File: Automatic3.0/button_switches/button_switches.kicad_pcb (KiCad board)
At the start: 2 copper layers, 37 parts, among them J1 DB9_Female_MountingHoles, J2 Conn_01x01, J3 Conn_01x01, J4 Conn_01x01, J5 Conn_01x01, SW1 SW_DPST, SW2 SW_DPST, SW3 SW_DPST, SW4 SW_DPST, SW5 SW_DPST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

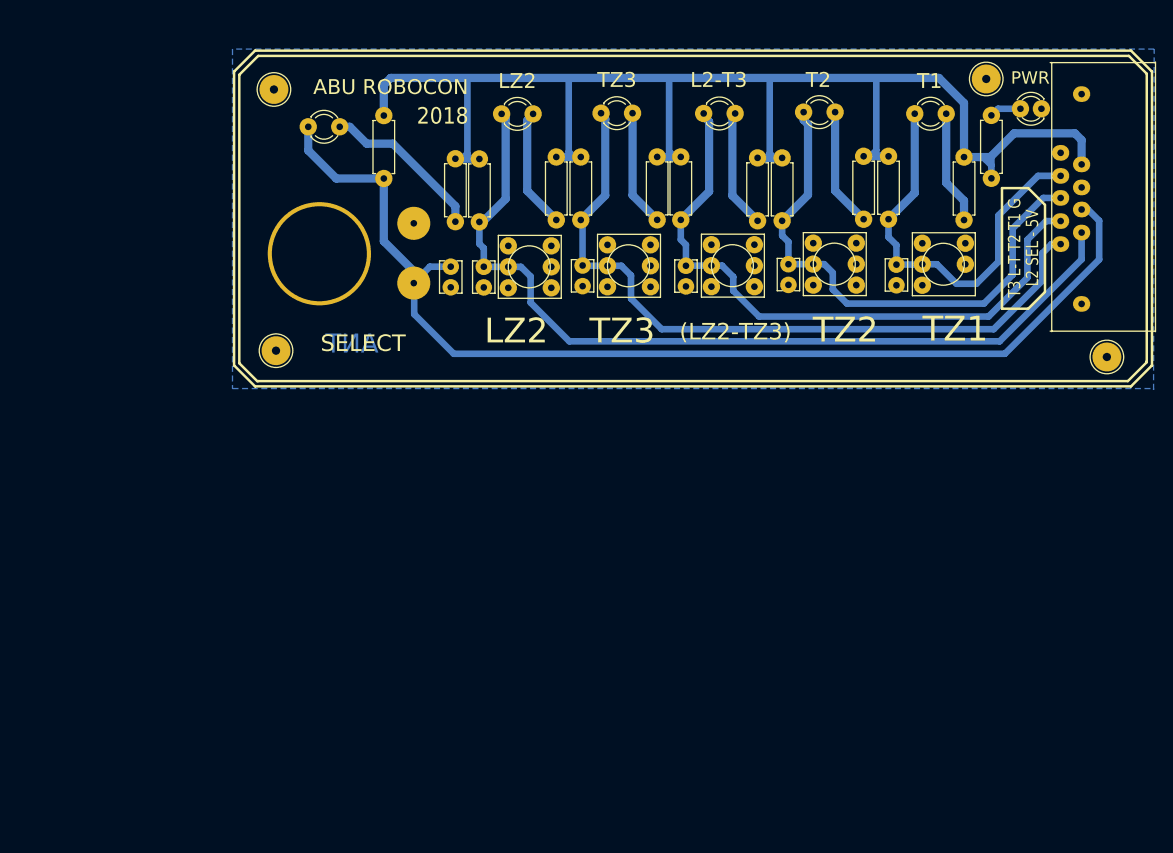
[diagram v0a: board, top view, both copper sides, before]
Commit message: added the minor project file
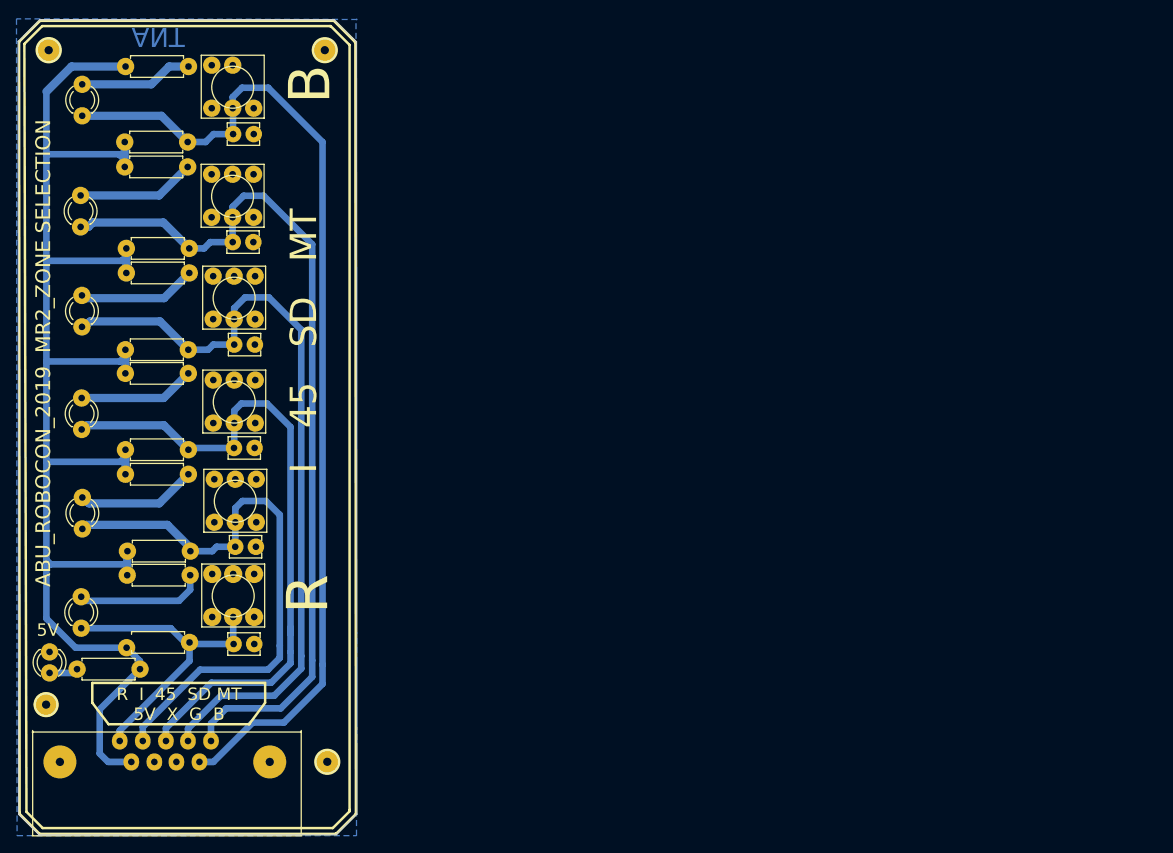
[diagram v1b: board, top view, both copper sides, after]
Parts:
- D1: value PWR -> 5V
- moved D1 136.9 mm to (69.4, 167.7), turned to 270 degrees
- moved R1 129.4 mm to (72.7, 169.8), turned to 0 degrees
- moved J1 125.1 mm to (88.9, 178.5), turned to 180 degrees
- moved J4 113.6 mm to (69.3, 94.8), turned to 90 degrees
- moved J5 101.7 mm to (102.7, 94.8), turned to 90 degrees
- moved D7 101.4 mm to (73.3, 102.1), turned to 90 degrees
- moved R7 95.7 mm to (86.2, 96.8), turned to 180 degrees
- moved D6 89.2 mm to (73.2, 115.6), turned to 90 degrees
- moved SW6 88.8 mm to (91.6, 99.2), turned to 0 degrees
- moved R14 85.4 mm to (86.1, 105.9), turned to 180 degrees
- moved R6 82.1 mm to (86.1, 109.0), turned to 180 degrees
- moved C6 81.8 mm to (91.6, 105.0), turned to 0 degrees
- moved D5 80.0 mm to (73.3, 127.7), turned to 90 degrees
- moved J2 79.4 mm to (69.0, 174.1), turned to 90 degrees
- moved D2 73.8 mm to (73.3, 140.1), turned to 90 degrees
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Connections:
- J1 pad 1: GND -> /IN5
- J1 pad 2: /IN6 -> /IN4
- J1 pad 3: /IN5 -> /IN1
- J1 pad 4: /IN4 -> /IN2
- J1 pad 5: /IN1 -> /IN3
- J1 pad 6: +5V -> /IN6
- J1 pad 7: (no net) -> GND
- J1 pad 8: /IN3 -> (no net)
- J1 pad 9: /IN2 -> +5V
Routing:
- net /IN3: track 133.7 -> 38.5 mm
- net /IN6: track 49.7 -> 123.1 mm
- net +5V: track 234.5 -> 177.3 mm
- net /IN5: track 65.0 -> 106.3 mm
- net /IN2: track 105.9 -> 70.7 mm
- net /IN4: track 76.8 -> 94.3 mm
- net /IN1: track 88.8 -> 82.1 mm
- net Net-(D4-Pad2): track 20.8 -> 15.7 mm
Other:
- board outline added: 41 x 98.7 mm
- net class Default: clearance 0.2 -> 0.45
- rule trace_clearance: 0.2 -> 0.45
- board text added: "ABU_ROBOCON_2019 MR2_ZONE SELECTION"
- board text added: "B"
- board text added: "I 45 SD MT"
- board text added: "R"
- board text added: "R I 45 SD MT 5V X G B"
- board text removed: "(LZ2-TZ3)"
- board text removed: "2018"
- board text removed: "ABU ROBOCON"
- board text removed: "L2 SEL - 5V"
- board text removed: "L2-T3"
- board text removed: "LZ2"
- board text removed: "SELECT"
- board text removed: "T1"
- board text removed: "T2"
- board text removed: "T3 L-T T2 T1 G"
- board text removed: "TZ1"
- board text removed: "TZ2"
- board text removed: "TZ3"
